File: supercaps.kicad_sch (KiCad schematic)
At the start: 17 parts, among them J8 XT30_F, J9 XT30_F, Q10 2SAR587D3, Q9 2SCR587D3, U17 TLV9301xDBV

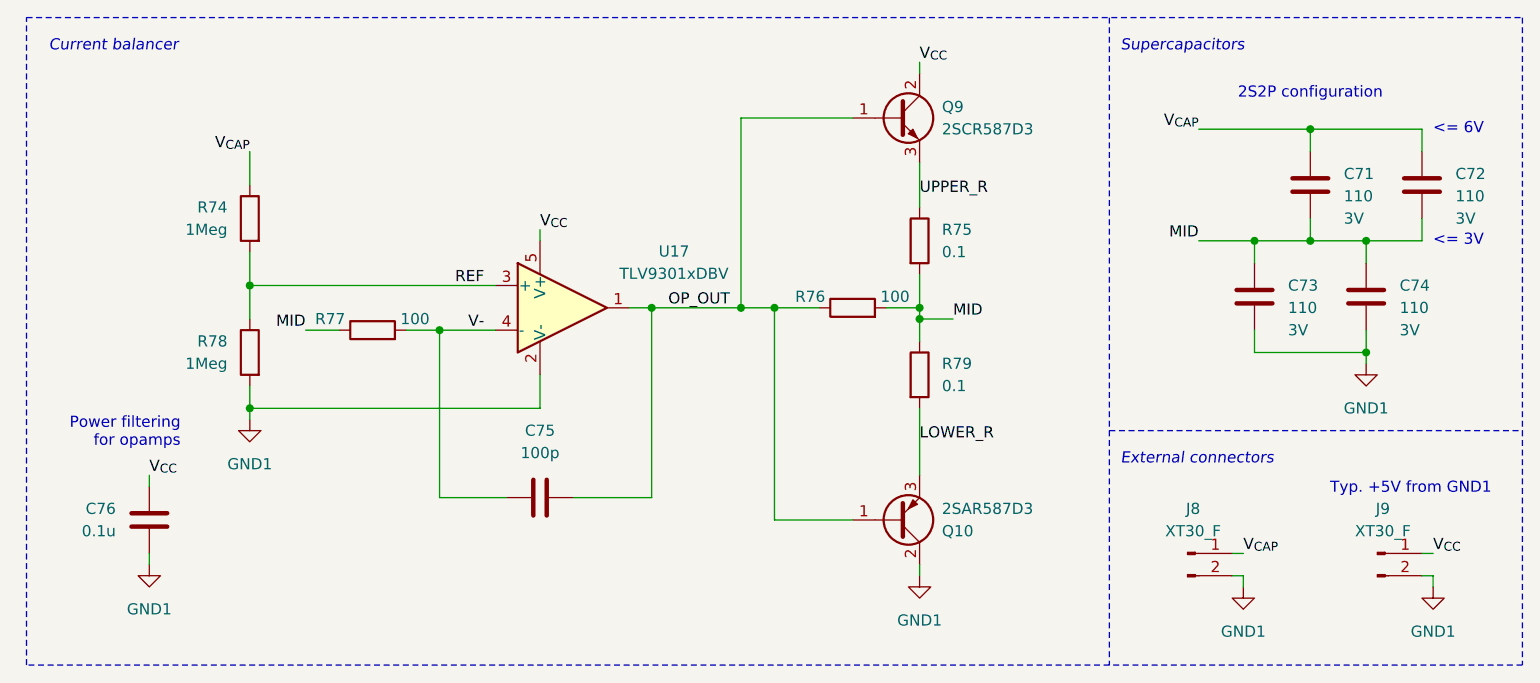
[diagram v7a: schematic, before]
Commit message: Specc'd all components + started creating rev 1b boards
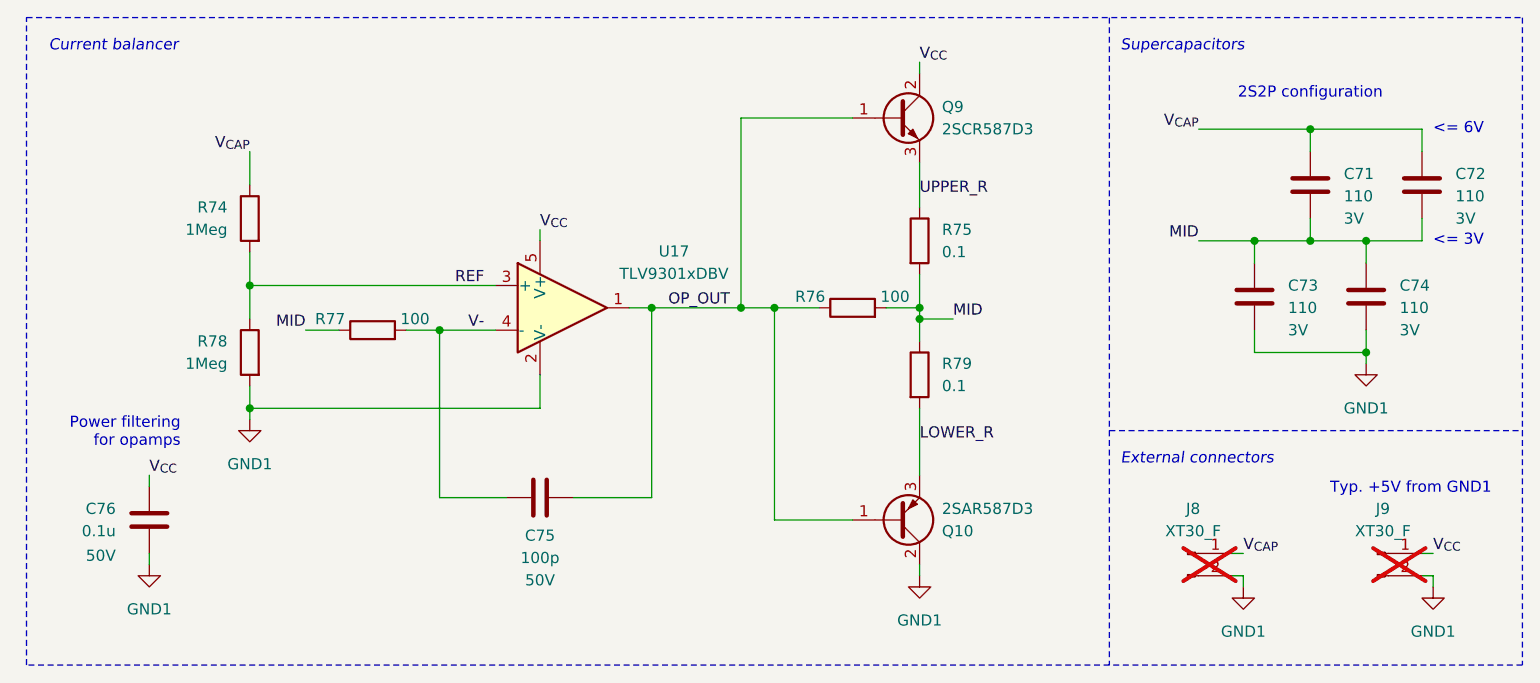
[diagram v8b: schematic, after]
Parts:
- C75: Mouser Part Number (none) -> 77-VJ0603A101KXACBC; Voltage Rating (none) -> 50V
- C76: Mouser Part Number (none) -> 581-KGM15BR71H104JT; Voltage Rating (none) -> 50V
- J8, J9: now not fitted
- R74, R78: Mouser Part Number 603-RC0603FR-1010ML -> 603-RC0603FR-071MP
- R76, R77: Mouser Part Number (none) -> 754-RG1608P-101DT5
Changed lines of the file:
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@@
 		(on_board yes)
 		(dnp no)
-		(fields_autoplaced yes)
 		(property "Reference" "C75"
-			(at 80.01 72.39 90)
+			(at 80.01 84.328 90)
 			(effects
 				(font
@@
 		)
 		(property "Value" "100p"
-			(at 80.01 74.93 90)
+			(at 80.01 86.868 90)
 			(effects
 				(font
@@
 				)
 				(hide yes)
+			)
+		)
+		(property "Mouser Part Number" "77-VJ0603A101KXACBC"
+			(at 80.01 80.01 0)
+			(effects
+				(font
+					(size 1.27 1.27)
+				)
+				(hide yes)
+			)
+		)
+		(property "Voltage Rating" "50V"
+			(at 80.01 89.408 90)
+			(effects
+				(font
+					(size 1.27 1.27)
+				)
 			)
 		)
@@
 		(on_board yes)
 		(dnp no)
-		(fields_autoplaced yes)
 		(property "Reference" "C76"
 			(at 31.75 81.2799 0)
@@
 			)
 		)
-		(property "Datasheet" "~"
+		(property "Datasheet" "https://www.mouser.com/datasheet/2/40/KGM_X7R-3223212.pdf"
 			(at 35.56 82.55 0)
 			(effects
@@
 					(size 1.27 1.27)
 				)
+			)
+		)
+		(property "Mouser Part Number" "581-KGM15BR71H104JT"
+			(at 35.56 82.55 0)
+			(effects
+				(font
+					(size 1.27 1.27)
+				)
+				(hide yes)
+			)
+		)
+		(property "Voltage Rating" "50V"
+			(at 31.75 86.614 0)
+			(effects
+				(font
+					(size 1.27 1.27)
+				)
+				(justify left)
 			)
 		)
@@
 		(in_bom yes)
 		(on_board yes)
-		(dnp no)
+		(dnp yes)
 		(property "Reference" "J9"
 			(at 175.895 81.28 0)
@@
 			)
 		)
-		(property "Mouser Part Number" "603-RC0603FR-1010ML"
+		(property "Mouser Part Number" "603-RC0603FR-071MP"
 			(at 46.99 48.26 0)
 			(effects
@@
 		(in_bom yes)
 		(on_board yes)
-		(dnp no)
+		(dnp yes)
 		(property "Reference" "J8"
 			(at 154.305 81.28 0)
@@
 			)
 		)
-		(property "Mouser Part Number" "603-RC0603FR-1010ML"
+		(property "Mouser Part Number" "603-RC0603FR-071MP"
 			(at 46.99 63.5 0)
 			(effects
@@
 		)
 		(property "Description" "Resistor"
+			(at 60.96 60.96 0)
+			(effects
+				(font
+					(size 1.27 1.27)
+				)
+				(hide yes)
+			)
+		)
+		(property "Mouser Part Number" "754-RG1608P-101DT5"
 			(at 60.96 60.96 0)
 			(effects
@@
 			(at 115.57 58.42 0)
 			(effects
+				(font
+					(size 1.27 1.27)
+				)
+				(hide yes)
+			)
+		)
+		(property "Mouser Part Number" "754-RG1608P-101DT5"
+			(at 115.57 58.42 0)
+			(effects
